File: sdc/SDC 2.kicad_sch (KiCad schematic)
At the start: 85 parts, among them J1 Conn_02x10_Odd_Even, K1 G2RL-2A, K2 G2RL-2A, K3 G2RL-2A, K4 G2RL-2A, Q1 2N7002, Q2 2N7002, Q3 2N7002, Q4 2N7002, Q5 2N7002, Q6 2N7002, U1 VOM618AT, U10 AP2204K-ADJ, U2 VOM618AT, U3 TLV2371DBV, U4 TLV2371DBV, U6 VOM618AT, U7 VOM618AT, U8 TLV2371DBV, U9 AP2204K-ADJ

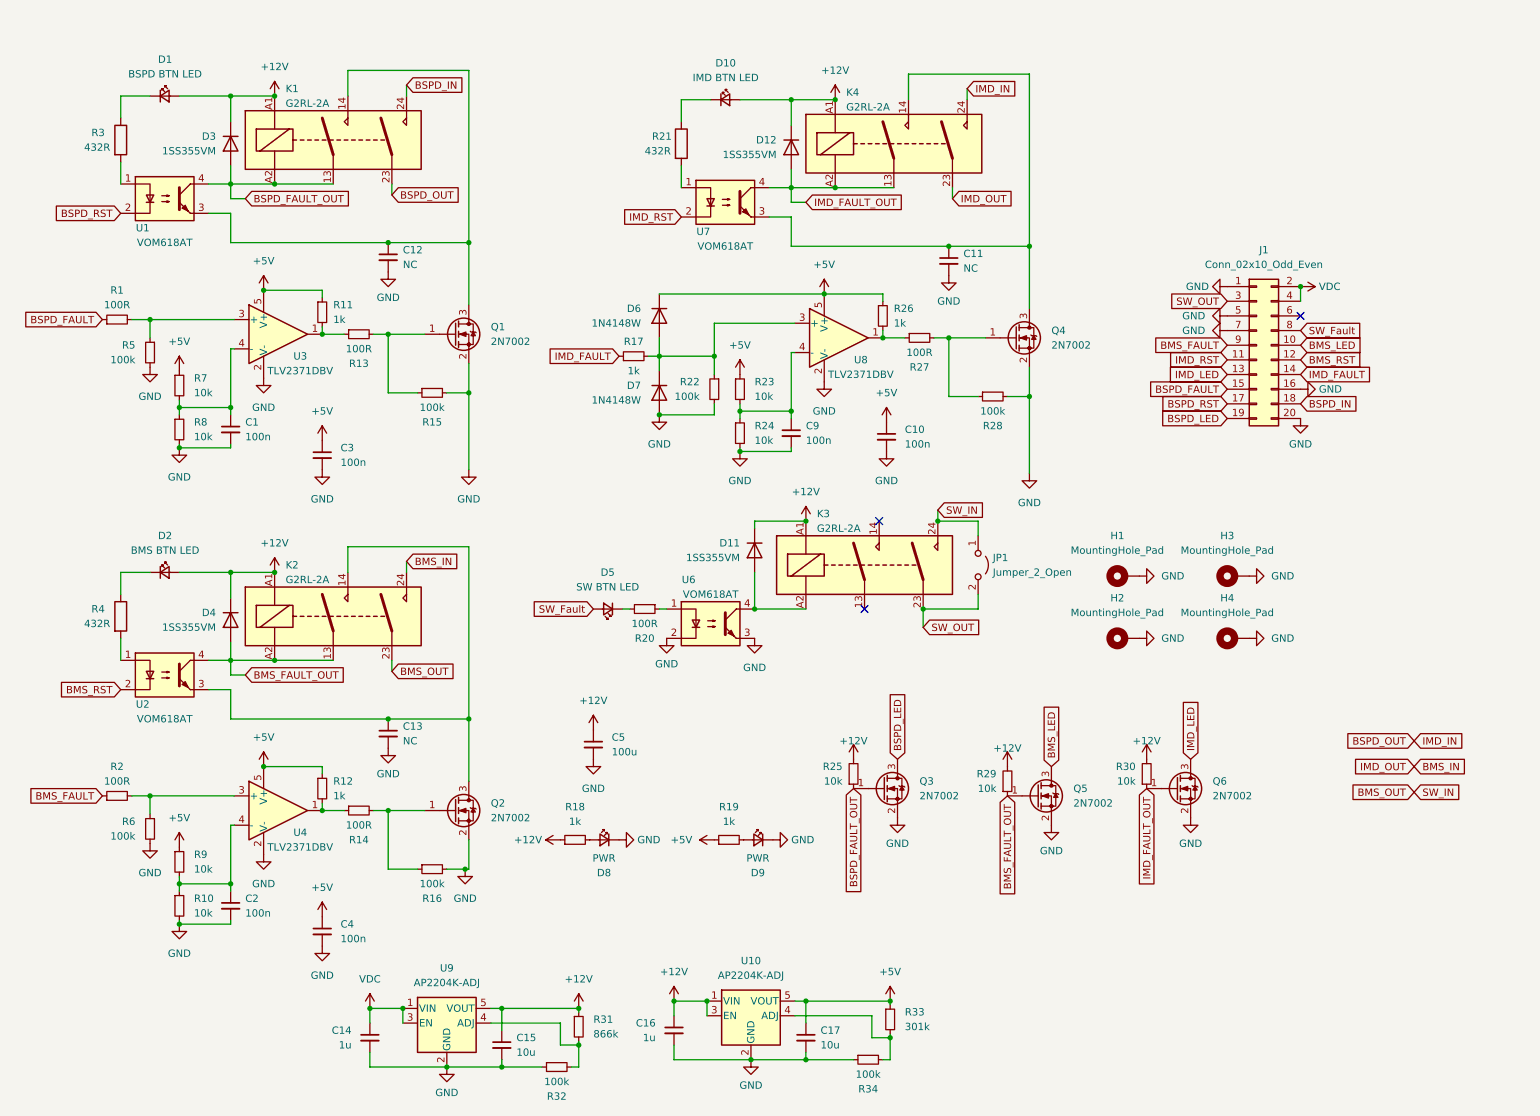
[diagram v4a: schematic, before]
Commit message: chore: remove pull up resistor and change flyback diodes
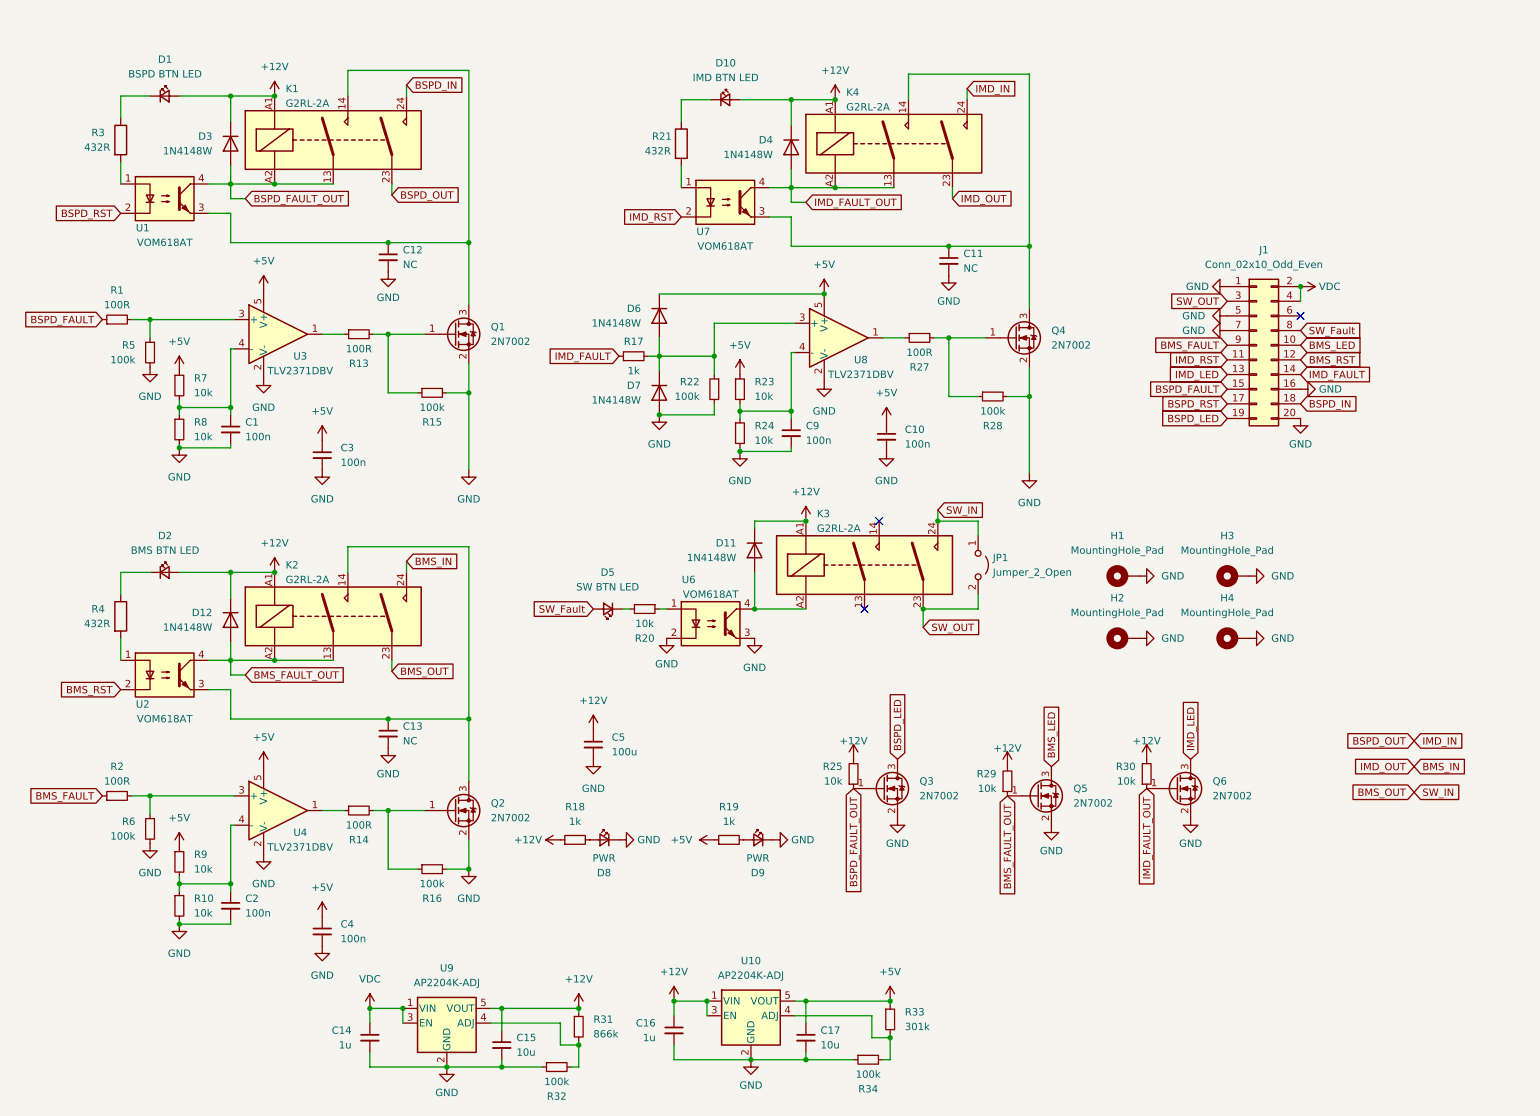
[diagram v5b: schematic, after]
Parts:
- removed D11, D12, D3, D4: 1SS355VM, Diode_SMD:D_SOD-323F, symbol Diode:1SS355VM
- removed R11, R12, R26: 1k, Resistor_SMD:R_0603_1608Metric, symbol Device:R_Small
- added D11, D12, D3, D4: 1N4148W, Diode_SMD:D_SOD-123, symbol Diode:1N4148W
- R20: value 100R -> 10k
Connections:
- net +12V: now also D11.1 (K), D12.1 (K), D3.1 (K), D4.1 (K)
- net BMS_FAULT_OUT: now also D12.2 (A)
- net BSPD_FAULT_OUT: now also D3.2 (A)
- net IMD_FAULT_OUT: now also D4.2 (A)
- net at K3.A2, U6.4: now also D11.2 (A)

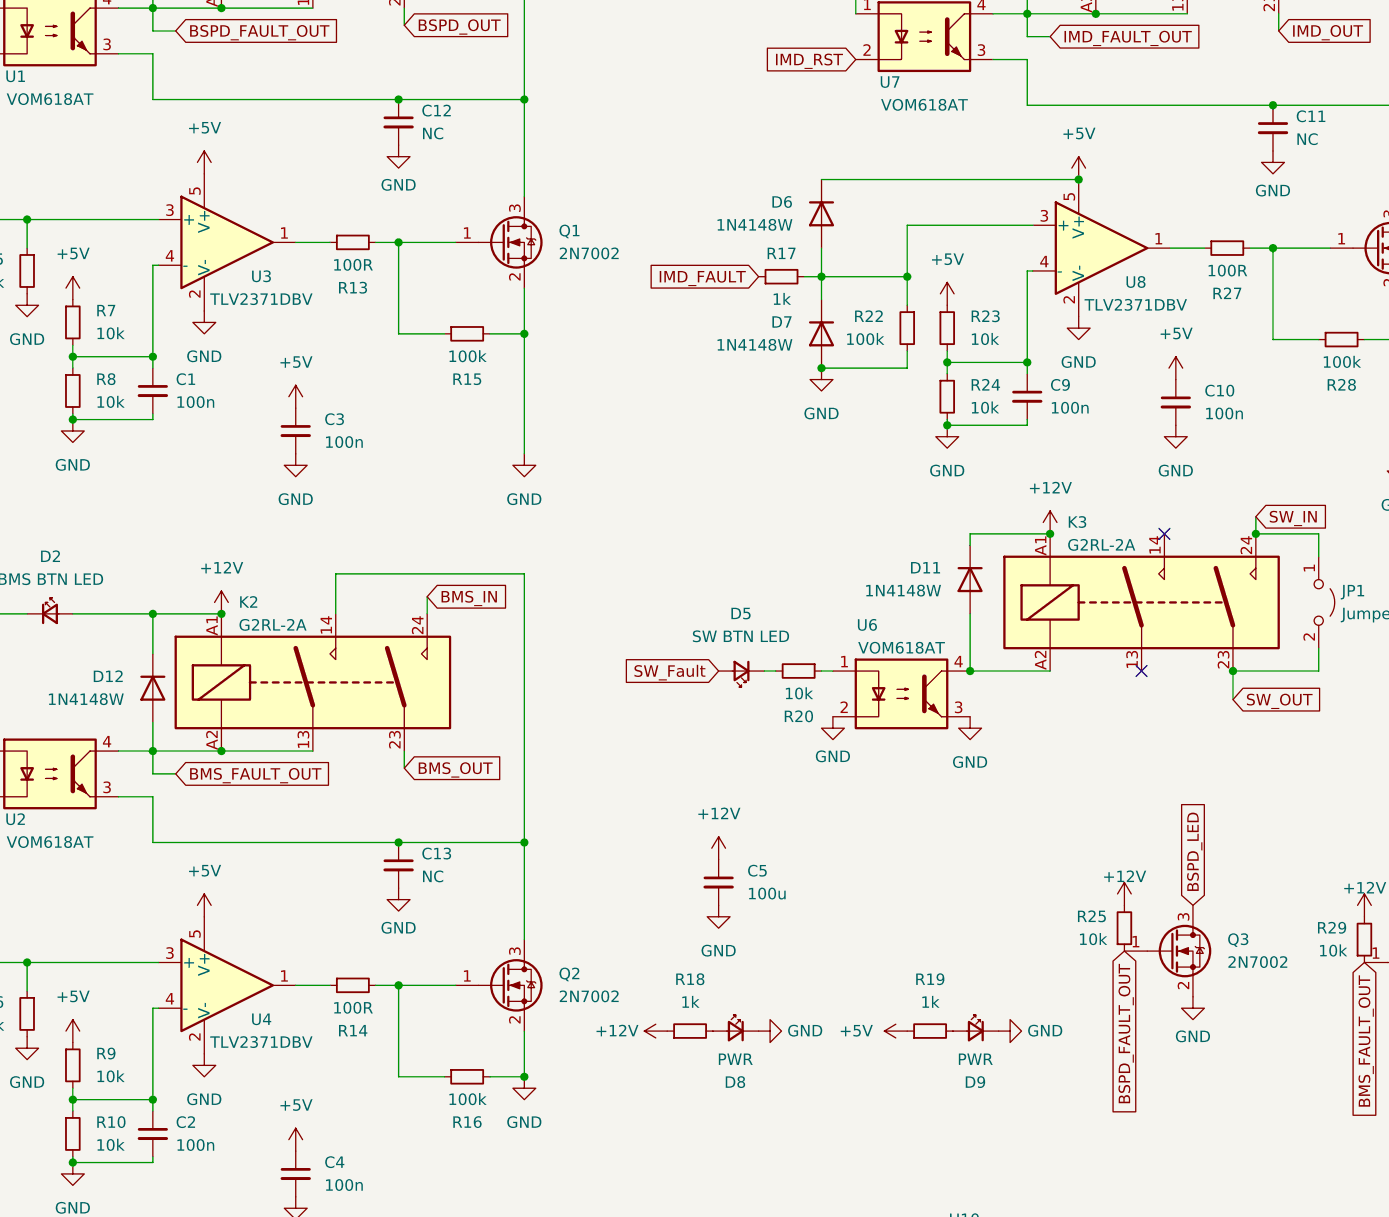
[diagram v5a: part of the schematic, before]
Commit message: change comparator to AS331KTR-G1
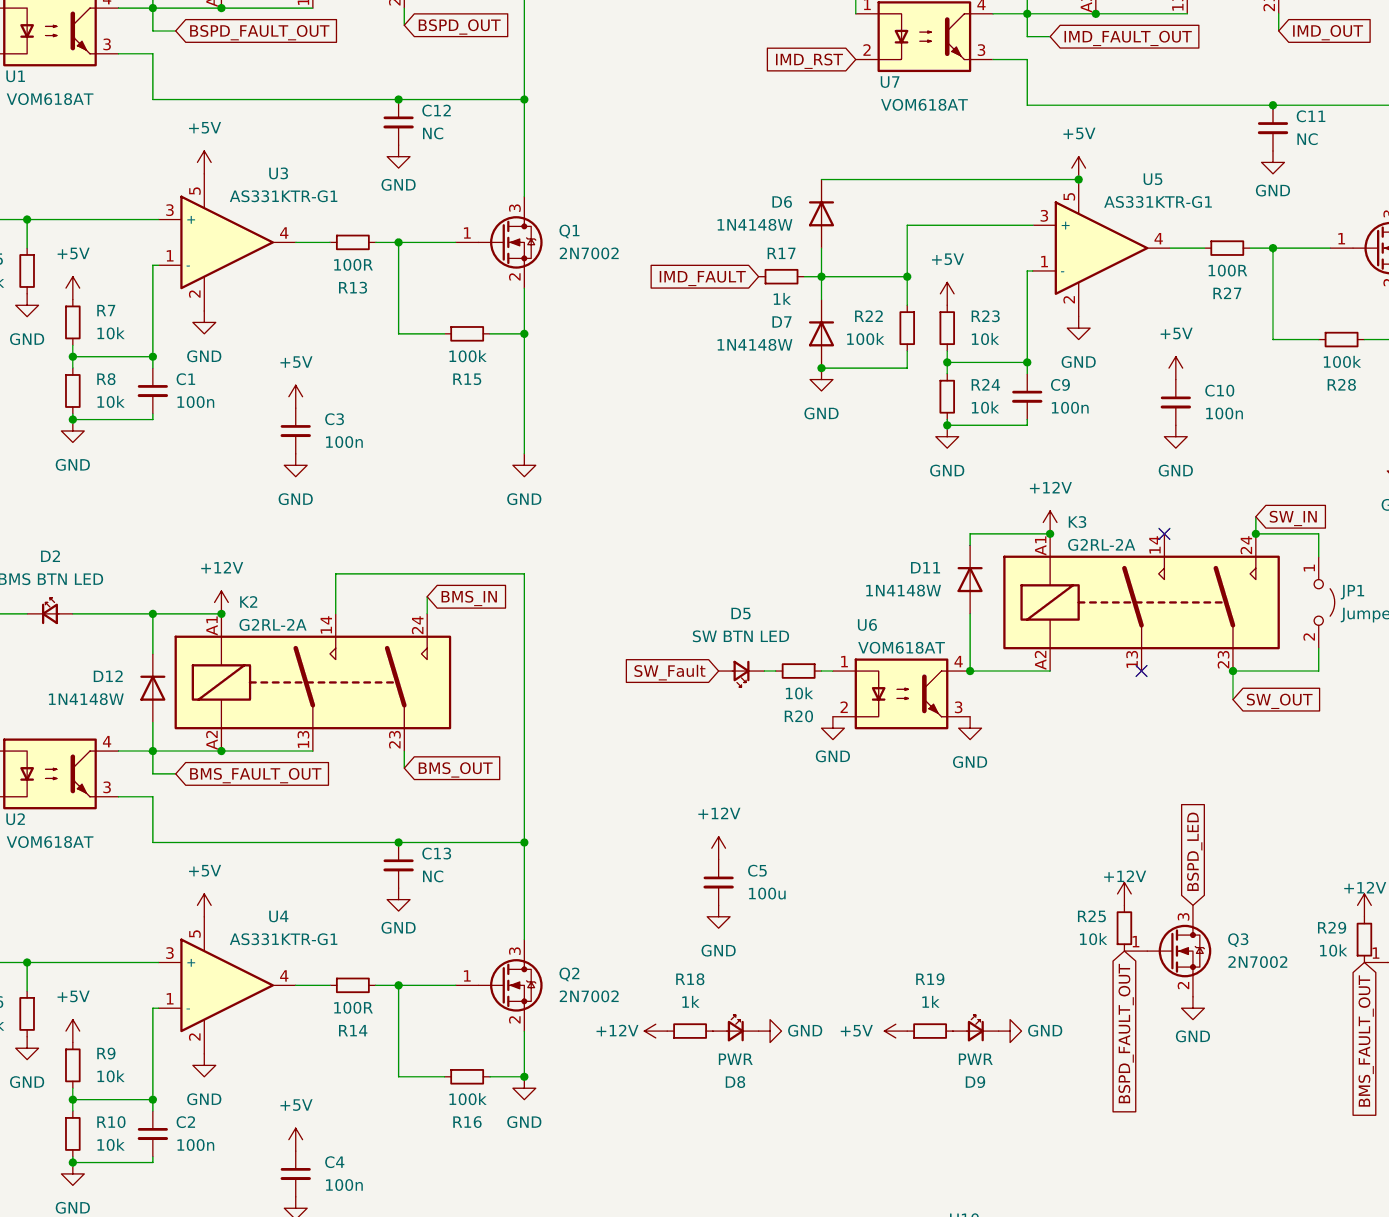
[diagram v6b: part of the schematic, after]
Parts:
- removed U3, U4, U8: TLV2371DBV, Package_TO_SOT_SMD:SOT-23-5, symbol Amplifier_Operational:TLV2371DBV
- added U3, U4, U5: AS331KTR-G1, Package_TO_SOT_SMD:SOT-23-5, symbol Comparator_AS331KTR-G1:AS331KTR-G1
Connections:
- net +5V: now also U3.5, U4.5, U5.5
- net GND: now also U3.2, U4.2, U5.2
- net at C2.1, R10.1, R9.2: now also U4.1 (-)
- net at D6.2 (A), D7.1 (K), R17.2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: now also U5.3 (+)
- net at R27.1: now also U5.4
- net at R2.2, R6.1: now also U4.3 (+)
- net at C9.1, R23.2, R24.1: now also U5.1 (-)
- net at C1.1, R7.2, R8.1: now also U3.1 (-)
- net at R14.1: now also U4.4
- net at R13.1: now also U3.4
- net at R1.2, R5.1: now also U3.3 (+)
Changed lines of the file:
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@@
   (title_block
     (title "SDC")
-    (date "2025-03-12")
+    (date "2025-07-23")
+    (rev "2025.07")
     (company "NCKU Formula Racing Team")
   )
@@
   (junction (at 137.16 180.34) (diameter 0) (color 0 0 0 0)
   )
-  (junction (at 157.48 57.785) (diameter 0) (color 0 0 0 0)
-  )
   (junction (at 81.915 147.32) (diameter 0) (color 0 0 0 0)
   )
+  (junction (at 157.48 57.785) (diameter 0) (color 0 0 0 0)
+  )
   (junction (at 179.07 49.53) (diameter 0) (color 0 0 0 0)
   )
@@
     )
   )
-  (symbol (lib_id "Amplifier_Operational:TLV2371DBV") (at 160.02 65.405 0) (unit 1)
-    (in_bom yes) (on_board yes) (dnp no)
-    (property "Reference" "U8" (at 163.83 69.215 0)
-      (effects (font (size 1.27 1.27)))
-    )
-    (property "Value" "TLV2371DBV" (at 163.83 71.755 0)
-      (effects (font (size 1.27 1.27)))
-    )
-    (property "Footprint" "Package_TO_SOT_SMD:SOT-23-5" (at 157.48 70.485 0)
-      (effects (font (size 1.27 1.27)) (justify left) hide)
-    )
-    (property "Datasheet" "http://www.ti.com/lit/ds/symlink/tlv2375.pdf" (at 160.02 60.325 0)
-      (effects (font (size 1.27 1.27)) hide)
-    )
-    (property "Sim.Library" "sloc062d/tlv2371.lib" (at 160.02 65.405 0)
-      (effects (font (size 1.27 1.27)) hide)
-    )
-    (property "Sim.Name" "TLV2371" (at 160.02 65.405 0)
-      (effects (font (size 1.27 1.27)) hide)
-    )
-    (property "Sim.Device" "SUBCKT" (at 160.02 65.405 0)
-      (effects (font (size 1.27 1.27)) hide)
-    )
-    (property "Sim.Pins" "1=3 2=4 3=6 4=2 5=1" (at 160.02 65.405 0)
-      (effects (font (size 1.27 1.27)) hide)
-    )
-    (pin "4")
-    (pin "5")
-    (pin "2")
-    (pin "1")
-    (pin "3")
-    (instances
-      (project "SDC 2"
-        (path "/5dfd26ec-2ec4-449e-a223-7366b4f866d8"
-          (reference "U8") (unit 1)
-        )
-      )
-    )
-  )
   (symbol (lib_id "Mechanical:MountingHole_Pad") (at 228.6 106.68 90) (unit 1)
     (in_bom yes) (on_board yes) (dnp no) (fields_autoplaced)
@@
     )
   )
+  (symbol (lib_id "Comparator_AS331KTR-G1:AS331KTR-G1") (at 60.325 147.32 0) (unit 1)
+    (in_bom yes) (on_board yes) (dnp no)
+    (property "Reference" "U4" (at 68.58 139.7 0)
+      (effects (font (size 1.27 1.27)))
+    )
+    (property "Value" "AS331KTR-G1" (at 69.215 142.24 0)
+      (effects (font (size 1.27 1.27)))
+    )
+    (property "Footprint" "Package_TO_SOT_SMD:SOT-23-5" (at 60.325 147.32 0)
+      (effects (font (size 1.27 1.27)) hide)
+    )
+    (property "Datasheet" "" (at 60.325 147.32 0)
+      (effects (font (size 1.27 1.27)) hide)
+    )
+    (pin "1")
+    (pin "2")
+    (pin "3")
+    (pin "4")
+    (pin "5")
+    (instances
+      (project "SDC 2"
+        (path "/5dfd26ec-2ec4-449e-a223-7366b4f866d8"
+          (reference "U4") (unit 1)
+        )
+      )
+    )
+  )
   (symbol (lib_id "power:+5V") (at 45.72 71.12 0) (unit 1)
     (in_bom yes) (on_board yes) (dnp no) (fields_autoplaced)
@@
     )
   )
-  (symbol (lib_id "Amplifier_Operational:TLV2371DBV") (at 62.865 147.32 0) (unit 1)
-    (in_bom yes) (on_board yes) (dnp no)
-    (property "Reference" "U4" (at 66.675 151.13 0)
-      (effects (font (size 1.27 1.27)))
-    )
-    (property "Value" "TLV2371DBV" (at 66.675 153.67 0)
-      (effects (font (size 1.27 1.27)))
-    )
-    (property "Footprint" "Package_TO_SOT_SMD:SOT-23-5" (at 60.325 152.4 0)
-      (effects (font (size 1.27 1.27)) (justify left) hide)
-    )
-    (property "Datasheet" "http://www.ti.com/lit/ds/symlink/tlv2375.pdf" (at 62.865 142.24 0)
-      (effects (font (size 1.27 1.27)) hide)
-    )
-    (property "Sim.Library" "sloc062d/tlv2371.lib" (at 62.865 147.32 0)
-      (effects (font (size 1.27 1.27)) hide)
-    )
-    (property "Sim.Name" "TLV2371" (at 62.865 147.32 0)
-      (effects (font (size 1.27 1.27)) hide)
-    )
-    (property "Sim.Device" "SUBCKT" (at 62.865 147.32 0)
-      (effects (font (size 1.27 1.27)) hide)
-    )
-    (property "Sim.Pins" "1=3 2=4 3=6 4=2 5=1" (at 62.865 147.32 0)
-      (effects (font (size 1.27 1.27)) hide)
-    )
-    (pin "4")
-    (pin "5")
-    (pin "2")
-    (pin "1")
-    (pin "3")
-    (instances
-      (project "SDC 2"
-        (path "/5dfd26ec-2ec4-449e-a223-7366b4f866d8"
-          (reference "U4") (unit 1)
-        )
-      )
-    )
-  )
-  (symbol (lib_id "Amplifier_Operational:TLV2371DBV") (at 62.865 64.77 0) (unit 1)
-    (in_bom yes) (on_board yes) (dnp no)
-    (property "Reference" "U3" (at 66.675 68.58 0)
-      (effects (font (size 1.27 1.27)))
-    )
-    (property "Value" "TLV2371DBV" (at 66.675 71.12 0)
-      (effects (font (size 1.27 1.27)))
-    )
-    (property "Footprint" "Package_TO_SOT_SMD:SOT-23-5" (at 60.325 69.85 0)
-      (effects (font (size 1.27 1.27)) (justify left) hide)
-    )
-    (property "Datasheet" "http://www.ti.com/lit/ds/symlink/tlv2375.pdf" (at 62.865 59.69 0)
-      (effects (font (size 1.27 1.27)) hide)
-    )
-    (property "Sim.Library" "sloc062d/tlv2371.lib" (at 62.865 64.77 0)
-      (effects (font (size 1.27 1.27)) hide)
-    )
-    (property "Sim.Name" "TLV2371" (at 62.865 64.77 0)
-      (effects (font (size 1.27 1.27)) hide)
-    )
-    (property "Sim.Device" "SUBCKT" (at 62.865 64.77 0)
-      (effects (font (size 1.27 1.27)) hide)
-    )
-    (property "Sim.Pins" "1=3 2=4 3=6 4=2 5=1" (at 62.865 64.77 0)
-      (effects (font (size 1.27 1.27)) hide)
-    )
-    (pin "4")
-    (pin "5")
-    (pin "2")
-    (pin "1")
-    (pin "3")
-    (instances
-      (project "SDC 2"
-        (path "/5dfd26ec-2ec4-449e-a223-7366b4f866d8"
-          (reference "U3") (unit 1)
-        )
-      )
-    )
-  )
   (symbol (lib_id "power:GND") (at 95.885 157.48 0) (unit 1)
     (in_bom yes) (on_board yes) (dnp no) (fields_autoplaced)
@@
     )
   )
+  (symbol (lib_id "Comparator_AS331KTR-G1:AS331KTR-G1") (at 157.48 65.405 0) (unit 1)
+    (in_bom yes) (on_board yes) (dnp no)
+    (property "Reference" "U5" (at 165.735 57.785 0)
+      (effects (font (size 1.27 1.27)))
+    )
+    (property "Value" "AS331KTR-G1" (at 166.37 60.325 0)
+      (effects (font (size 1.27 1.27)))
+    )
+    (property "Footprint" "Package_TO_SOT_SMD:SOT-23-5" (at 157.48 65.405 0)
+      (effects (font (size 1.27 1.27)) hide)
+    )
+    (property "Datasheet" "" (at 157.48 65.405 0)
+      (effects (font (size 1.27 1.27)) hide)
+    )
+    (pin "1")
+    (pin "2")
+    (pin "3")
+    (pin "4")
+    (pin "5")
+    (instances
+      (project "SDC 2"
+        (path "/5dfd26ec-2ec4-449e-a223-7366b4f866d8"
+          (reference "U5") (unit 1)
+        )
+      )
+    )
+  )
   (symbol (lib_id "Relay:G2RL-2A") (at 169.545 31.75 0) (unit 1)
     (in_bom yes) (on_board yes) (dnp no)
@@
         )
       )
+    )
+  )
+  (symbol (lib_id "Comparator_AS331KTR-G1:AS331KTR-G1") (at 60.325 64.77 0) (unit 1)
+    (in_bom yes) (on_board yes) (dnp no)
+    (property "Reference" "U3" (at 68.58 57.15 0)
+      (effects (font (size 1.27 1.27)))
+    )
+    (property "Value" "AS331KTR-G1" (at 69.215 59.69 0)
+      (effects (font (size 1.27 1.27)))
+    )
+    (property "Footprint" "Package_TO_SOT_SMD:SOT-23-5" (at 60.325 64.77 0)
+      (effects (font (size 1.27 1.27)) hide)
+    )
+    (property "Datasheet" "" (at 60.325 64.77 0)
+      (effects (font (size 1.27 1.27)) hide)
+    )
+    (pin "1")
+    (pin "2")
+    (pin "3")
+    (pin "4")
+    (pin "5")
+    (instances
+      (project "SDC 2"
+        (path "/5dfd26ec-2ec4-449e-a223-7366b4f866d8"
+          (reference "U3") (unit 1)
+        )
+      )
